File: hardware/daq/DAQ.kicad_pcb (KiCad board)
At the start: 2 copper layers, 114.9 x 120 mm, 131 parts, among them P1 0022272021, U1 ADS124S08IRHBT, U2 ADS124S08IRHBT, U3 LT6654BMPS6-5-TRMPBF, U4 LM1086IS-5.0_NOPB, U5 TPS73801DCQR, U6 TPSM63603RDHR, U7 TPSM63603RDHR, U8 TPSM63603RDHR

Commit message: FIXED ALL OF THE STUPID FOOTPRINT ISSUES
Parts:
- added C75: 16nF, GRM3195C2A163JA01D:CAPC3216X95N, F.Cu at (251.5, 66.3)
- added C76: 16nF, GRM3195C2A163JA01D:CAPC3216X95N, F.Cu at (251.5, 69.6)
- added C77: 16nF, GRM3195C2A163JA01D:CAPC3216X95N, F.Cu at (251.5, 72.9)
- added C78: 16nF, GRM3195C2A163JA01D:CAPC3216X95N, F.Cu at (251.5, 76.2)
- added C79: 16nF, GRM3195C2A163JA01D:CAPC3216X95N, F.Cu at (251.5, 79.5)
- added C80: 16nF, GRM3195C2A163JA01D:CAPC3216X95N, F.Cu at (251.5, 82.9)
- added C81: 16nF, GRM3195C2A163JA01D:CAPC3216X95N, F.Cu at (251.5, 86.2)
- added C82: 16nF, GRM3195C2A163JA01D:CAPC3216X95N, F.Cu at (251.5, 89.5)
- added C83: 16nF, GRM3195C2A163JA01D:CAPC3216X95N, F.Cu at (251.5, 92.8)
- added C84: 100nF, VJ0603Y104JXXAC:CAPC1608X97N, F.Cu at (256.2, 104.8)
- added C87: 10uF, GRM21BC71E106KE11L:CAPC2012X145N, F.Cu at (256.4, 96.0)
- added C88: 10uF, GRM21BC71E106KE11L:CAPC2012X145N, F.Cu at (256.4, 99.0)
- added C89: 1uF, 0603YC105JAT2A:CAPC1608X94N, F.Cu at (256.2, 114.9)
- added C90: 1uF, 0603YC105JAT2A:CAPC1608X94N, F.Cu at (256.2, 117.4)
- added C91: 100nF, VJ0603Y104JXXAC:CAPC1608X97N, F.Cu at (256.2, 107.3)
- added C92: 100nF, VJ0603Y104JXXAC:CAPC1608X97N, F.Cu at (256.2, 109.8)
- added C93: 10uF, GRM21BC71E106KE11L:CAPC2012X145N, F.Cu at (256.4, 102.0)
- added C94: 1uF, 0603YC105JAT2A:CAPC1608X94N, F.Cu at (256.2, 119.9)
- added C95: 100nF, VJ0603Y104JXXAC:CAPC1608X97N, F.Cu at (256.2, 112.3)
- added D1: ESDA6V1BC6, ESDA6V1BC6:SOT95P280X145-6N, F.Cu at (251.6, 96.7)
- added D2: ESDA6V1BC6, ESDA6V1BC6:SOT95P280X145-6N, F.Cu at (251.6, 101.2)
- added D3: ESDA6V1BC6, ESDA6V1BC6:SOT95P280X145-6N, F.Cu at (251.6, 105.7)
- added D4: ESDA6V1BC6, ESDA6V1BC6:SOT95P280X145-6N, F.Cu at (251.6, 110.1)
- added D5: ESDA6V1BC6, ESDA6V1BC6:SOT95P280X145-6N, F.Cu at (251.6, 114.6)
- added D6: ESDA6V1BC6, ESDA6V1BC6:SOT95P280X145-6N, F.Cu at (251.6, 119.1)
- added D7: SMS12T1G, SMST12T1G:SOT95P275X110-6N, F.Cu at (251.4, 128.1)
- added D8: ESDA6V1BC6, ESDA6V1BC6:SOT95P280X145-6N, F.Cu at (251.6, 123.6)
- added J1: ICD15S13E4GX00LF, ICD15S13:AMPHENOL_ICD15S13E4GX00LF, F.Cu at (169.1, 107.5)
- added J2: ICD15S13E4GX00LF, ICD15S13:AMPHENOL_ICD15S13E4GX00LF, F.Cu at (169.2, 75.9)
- added J3: ICD15S13E4GX00LF, ICD15S13:AMPHENOL_ICD15S13E4GX00LF, F.Cu at (169.1, 139.1)
- added J4: ICD15S13E4GX00LF, ICD15S13:AMPHENOL_ICD15S13E4GX00LF, F.Cu at (169.3, 44.3)
- added R27: 20K, CRCW060320K0FKEA:RESC1508X50N, F.Cu at (256.3, 65.9)
- added R28: 20K, CRCW060320K0FKEA:RESC1508X50N, F.Cu at (256.3, 68.4)
- added R3: 1.8k, Resistor_SMD:R_0603_1608Metric, F.Cu at (250.7, 40.4)
- added R4: 1.8K, Resistor_SMD:R_0603_1608Metric, F.Cu at (250.7, 42.9)
- added R43: 10k, Resistor_SMD:R_0603_1608Metric, F.Cu at (250.7, 45.4)
- added R44: 10k, Resistor_SMD:R_0603_1608Metric, F.Cu at (250.7, 47.9)
- added R45: 10k, Resistor_SMD:R_0603_1608Metric, F.Cu at (250.7, 50.4)
- added R46: 10k, Resistor_SMD:R_0603_1608Metric, F.Cu at (254.8, 40.4)
- added R47: 10k, Resistor_SMD:R_0603_1608Metric, F.Cu at (254.8, 42.9)
- added R48: 10k, Resistor_SMD:R_0603_1608Metric, F.Cu at (254.8, 45.4)
- added R49: 10k, Resistor_SMD:R_0603_1608Metric, F.Cu at (254.8, 47.9)
- added R50: 10k, Resistor_SMD:R_0603_1608Metric, F.Cu at (254.8, 50.4)
- added R51: 20K, CRCW060320K0FKEA:RESC1508X50N, F.Cu at (256.3, 70.9)
- added R52: 1K, CRCW060320K0FKEA:RESC1508X50N, F.Cu at (256.3, 73.5)
- added R53: 2.2K, CRCW060320K0FKEA:RESC1508X50N, F.Cu at (256.3, 76.0)
- added R54: 20K, CRCW060320K0FKEA:RESC1508X50N, F.Cu at (256.3, 78.5)
- added U11: SN74AHCT125RGYR, ul_SN74AHCT125RGYR:RGY14_2P05X2P05, F.Cu at (251.8, 61.6)
- added U9: ADS124S08IRHBT, ADS124S08IRHBT:QFN50P500X500X100-33N, F.Cu at (252.7, 55.2)
- R1, R10, R11, R12, R13, R14, R15, R16, R17, R18, R19, R2, R20, R21, R22, R23, R24, R5, R6, R7, R8, R9: footprint footprints10kR:RC0603N_YAG-M -> Resistor_SMD:R_0603_1608Metric
- RP1: value Raspberry_Pi_5 -> Raspberry_Pi_4
- U2: footprint footprintsADC:RHB0032M -> ADS124S08IRHBT:QFN50P500X500X100-33N
- moved H1 30.5 mm to (156.2, 32.0)
- moved H4 19.4 mm to (72.4, 150.9)
- moved C2 19.1 mm to (100.5, 144.6)
- moved C24 19.1 mm to (102.2, 129.3)
- moved C35 19.1 mm to (113.4, 129.8)
- moved C38 19.1 mm to (109.8, 132.0)
- moved C41 19.1 mm to (113.2, 146.0)
- moved C43 19.1 mm to (113.2, 143.6)
- moved C45 19.1 mm to (113.2, 141.4)
- moved G*** 19.1 mm to (74.1, 143.6)
- moved R1 19.1 mm to (96.9, 134.6)
- moved R2 19.1 mm to (96.3, 104.3)
- moved R41 19.1 mm to (109.0, 142.6)
- moved U2 19.1 mm to (111.2, 137.3)
- moved C8 19.1 mm to (121.3, 110.4)
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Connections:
- RP1 pad 10: unconnected-(RP1-GPIO_15/[UART]_RXD0-Pad10) -> /RX_PI
- RP1 pad 12: unconnected-(RP1-GPIO_18/PWM0/SPI1_CS0-Pad12) -> /DRDY_N3
- RP1 pad 15: /RESET_N1 -> /POFFV
- RP1 pad 16: unconnected-(RP1-GPIO_23-Pad16) -> /PWFV
- RP1 pad 22: /RESET_N2 -> /FTVV
- RP1 pad 29: unconnected-(RP1-GPIO5//GPCLK1-Pad29) -> /OIMV/FIMV/SPARK
- RP1 pad 3: unconnected-(RP1-GPIO_2/[I2C]_SDA-Pad3) -> /FMFV
- RP1 pad 31: unconnected-(RP1-GPIO6/GPCLK2-Pad31) -> /PFFFV
- RP1 pad 33: unconnected-(RP1-GPIO13/PWM1-Pad33) -> /TX_ENABLE
- RP1 pad 35: unconnected-(RP1-GPIO19/SPI0_MISO1/PWM1-Pad35) -> /OTVV
- RP1 pad 36: unconnected-(RP1-GPIO16/SPI1_CS2-Pad36) -> /CE3
- RP1 pad 38: unconnected-(RP1-GPIO20/SPI0_MOSI1-Pad38) -> /START_SYNC3
- RP1 pad 40: unconnected-(RP1-GPIO21/SPI0_SCLK1-Pad40) -> /WTVV
- RP1 pad 5: unconnected-(RP1-GPIO_3/[I2C]_SCL-Pad5) -> /OMFV
- RP1 pad 7: unconnected-(RP1-GPIO_4/GPCLK0-Pad7) -> /OFFV
- RP1 pad 8: unconnected-(RP1-GPIO_14/[UART]_TXD0-Pad8) -> /TX_PI
- U1 pad 18: /RESET_N1 -> Net-(U1-RESET_N)
- U1 pad V: GND -> (no net)
- U2 pad 18: /RESET_N2 -> Net-(U2-RESET_N)
- U6 pad 31: +5V -> (no net)
- U6 pad 32: GND -> (no net)
- U6 pad 33: GND -> (no net)
- U6 pad 34: GND -> (no net)
- U6 pad 35: GND -> (no net)
- U6 pad 36: GND -> (no net)
- U7 pad 31: +11V -> (no net)
- U7 pad 32: GND -> (no net)
- U7 pad 33: GND -> (no net)
- U7 pad 34: GND -> (no net)
- U7 pad 35: GND -> (no net)
- U7 pad 36: GND -> (no net)
- U8 pad 31: +6V -> (no net)
- U8 pad 32: GND -> (no net)
- U8 pad 33: GND -> (no net)
- U8 pad 34: GND -> (no net)
- U8 pad 35: GND -> (no net)
- U8 pad 36: GND -> (no net)
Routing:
- net 24V: track 55.7 -> 59.1 mm
- net /RESET_N2: vias 1 -> 0
- net Net-(U2-RESET_N): vias 0 -> 1
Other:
- board size 114.9 x 120 mm -> 112 x 126.6 mm

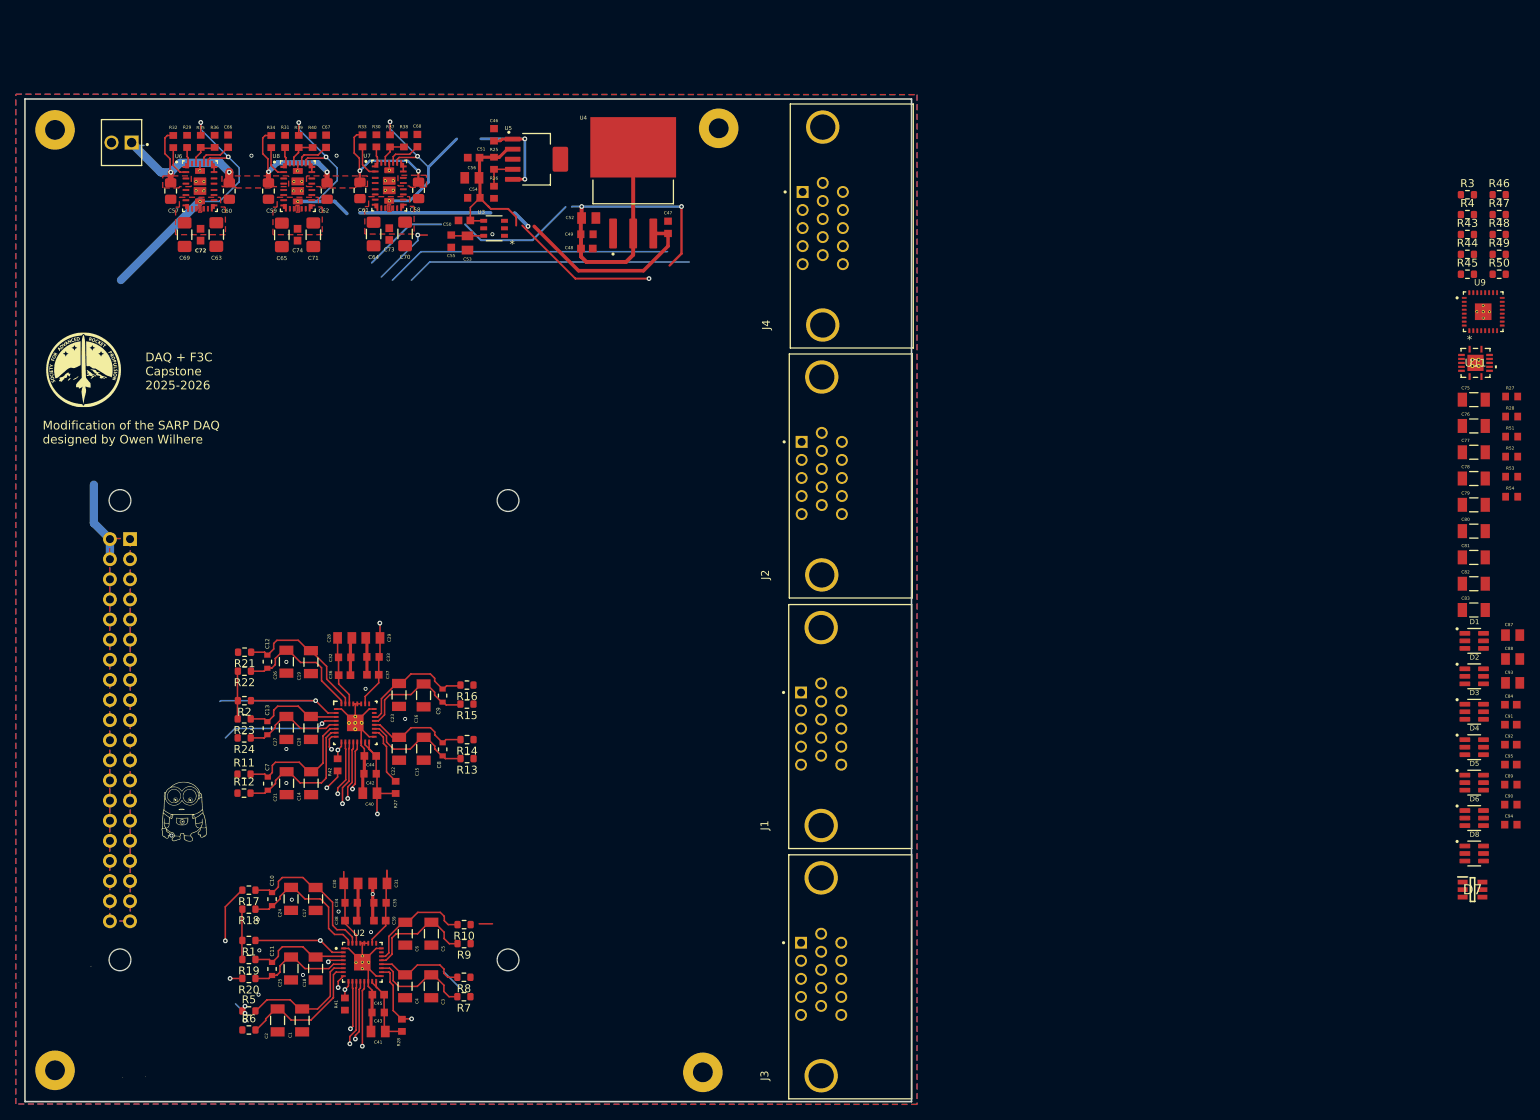
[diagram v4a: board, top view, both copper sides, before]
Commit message: starting to place 3rd ADC components
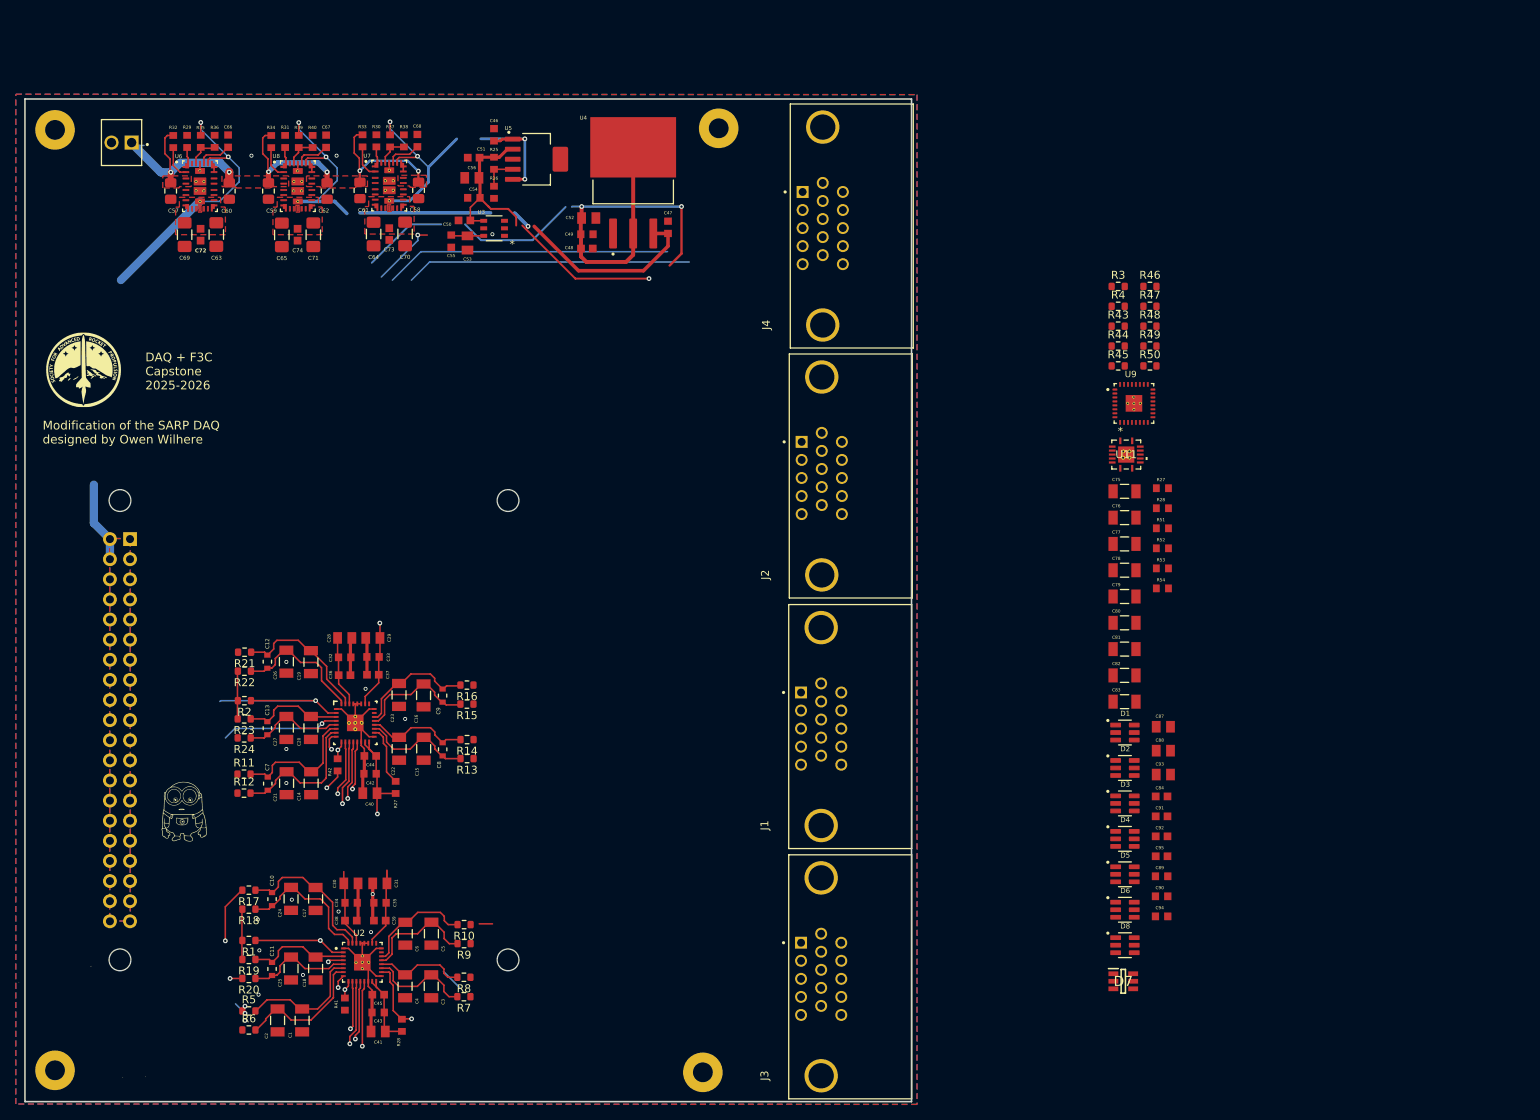
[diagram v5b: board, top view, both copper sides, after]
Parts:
- moved C84 45.6 mm to (212.1, 116.4)
- moved C92 45.6 mm to (212.1, 121.4)
- moved C95 45.6 mm to (212.1, 123.9)
- moved R3 45.6 mm to (206.6, 52.0)
- moved R4 45.6 mm to (206.6, 54.5)
- moved R43 45.6 mm to (206.6, 57.0)
- moved R44 45.6 mm to (206.6, 59.5)
- moved R45 45.6 mm to (206.6, 62.0)
- moved R52 45.6 mm to (212.2, 85.0)
- moved R53 45.6 mm to (212.2, 87.6)
- moved R54 45.6 mm to (212.2, 90.1)
- moved C89 45.6 mm to (212.1, 126.4)
- moved C90 45.6 mm to (212.1, 129.0)
- moved C91 45.6 mm to (212.1, 118.9)
- moved C94 45.6 mm to (212.1, 131.5)
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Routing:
- net GND: vias 17 -> 16

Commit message: lowkirk idk what I changed but I want to start working on my pc
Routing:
- net /PT6_SIG: track 1.69 -> 0.00 mm
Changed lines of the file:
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@@
+	)
+	(segment
+		(start 175.1845 85.9845)
+		(end 175.2 86)
+		(width 0.2)
+		(layer "F.Cu")
+		(net 36)
 	)
 	(segment
@@
 	)
 	(segment
-		(start 125.951952 132.452317)
-		(end 127.638618 132.452317)
-		(width 0.2)
-		(layer "F.Cu")
-		(net 47)
-	)
-	(segment

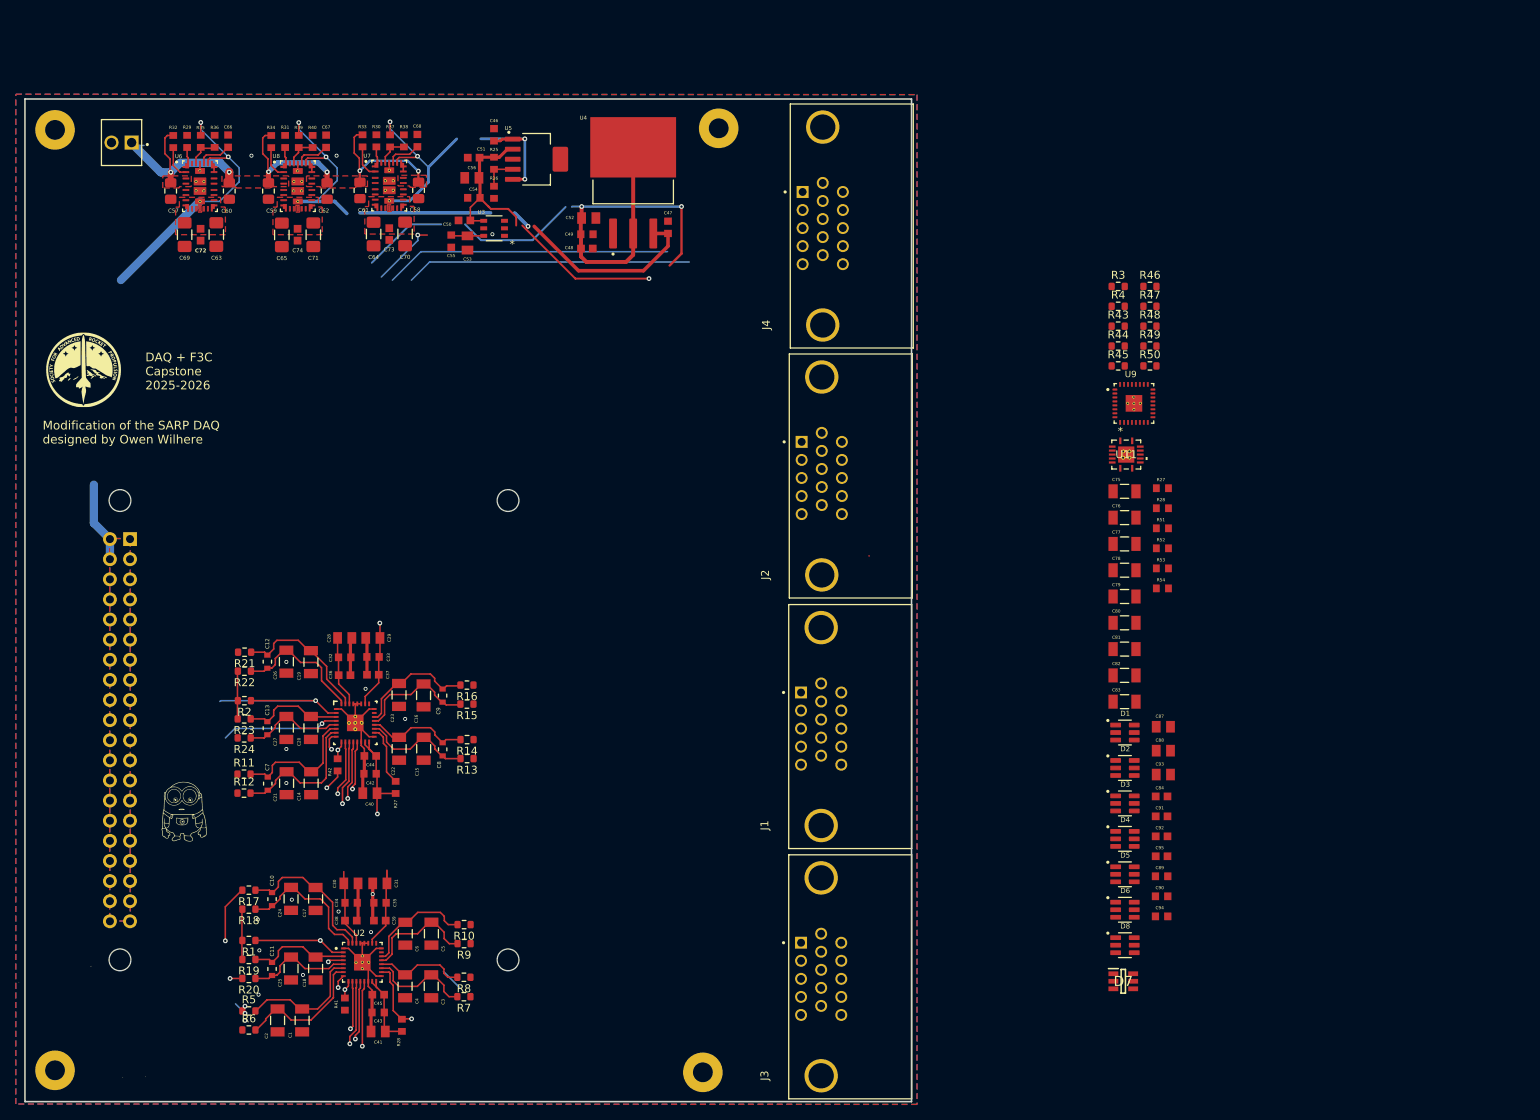
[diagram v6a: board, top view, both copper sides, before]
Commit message: re-mapped all DSUB pins
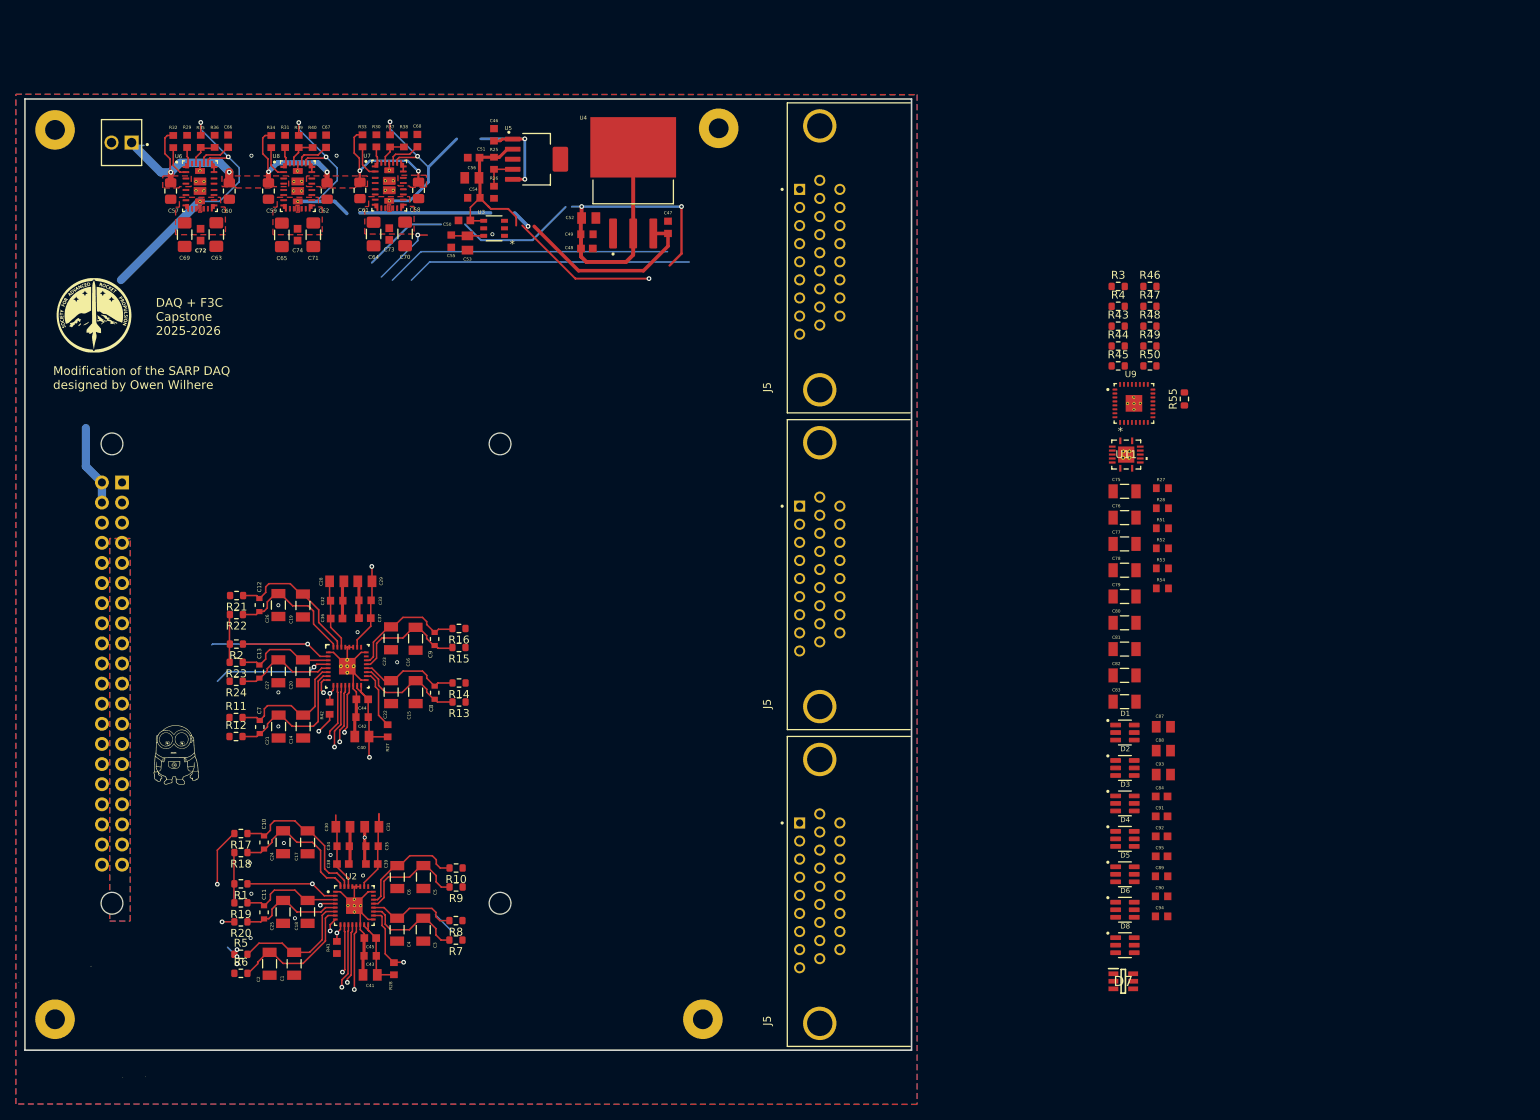
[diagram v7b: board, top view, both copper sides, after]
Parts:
- removed J1, J2, J3, J4: ICD15S13E4GX00LF, ICD15S13:AMPHENOL_ICD15S13E4GX00LF
- added J5: ICD26S13E4GX00LF, ICD26S13E4GX00LF:AMPHENOL_ICD26S13E4GX00LF, F.Cu at (169.0, 128.4)
- added J5: ICD26S13E4GX00LF, ICD26S13E4GX00LF:AMPHENOL_ICD26S13E4GX00LF, F.Cu at (169.0, 48.4)
- added J5: ICD26S13E4GX00LF, ICD26S13E4GX00LF:AMPHENOL_ICD26S13E4GX00LF, F.Cu at (169.0, 88.4)
- added R55: 10k, Resistor_SMD:R_0603_1608Metric, F.Cu at (215.0, 66.2)
- moved C34 7.22 mm to (108.8, 122.6)
- moved C38 7.22 mm to (108.7, 124.9)
- moved C39 7.22 mm to (112.4, 124.9)
- moved C35 7.22 mm to (112.4, 122.6)
- moved C1 7.22 mm to (102.6, 137.5)
- moved C13 7.22 mm to (98.2, 100.6)
- moved C15 7.22 mm to (117.9, 103.2)
- moved C16 7.22 mm to (117.9, 96.5)
- moved C19 7.22 mm to (103.7, 92.3)
- moved C2 7.22 mm to (99.5, 137.5)
- moved C20 7.22 mm to (103.7, 100.6)
- moved C24 7.22 mm to (101.2, 122.2)
- moved C25 7.22 mm to (101.2, 130.9)
- moved C27 7.22 mm to (100.6, 100.6)
- moved C3 7.22 mm to (118.9, 133.2)
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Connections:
- net /PT15_SIG renamed Net-(U9-GPIO0_AIN8)
- D1 pad 6: +5Vs -> /PT6_POW+
- D2 pad 4: +5Vs -> /PT5_POW+
- D2 pad 6: +5Vs -> /PT4_POW+
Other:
- board size 112 x 126.6 mm -> 112 x 120.1 mm
